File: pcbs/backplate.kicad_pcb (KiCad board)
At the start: 2 copper layers, 171.6 x 164.6 mm, 9 parts

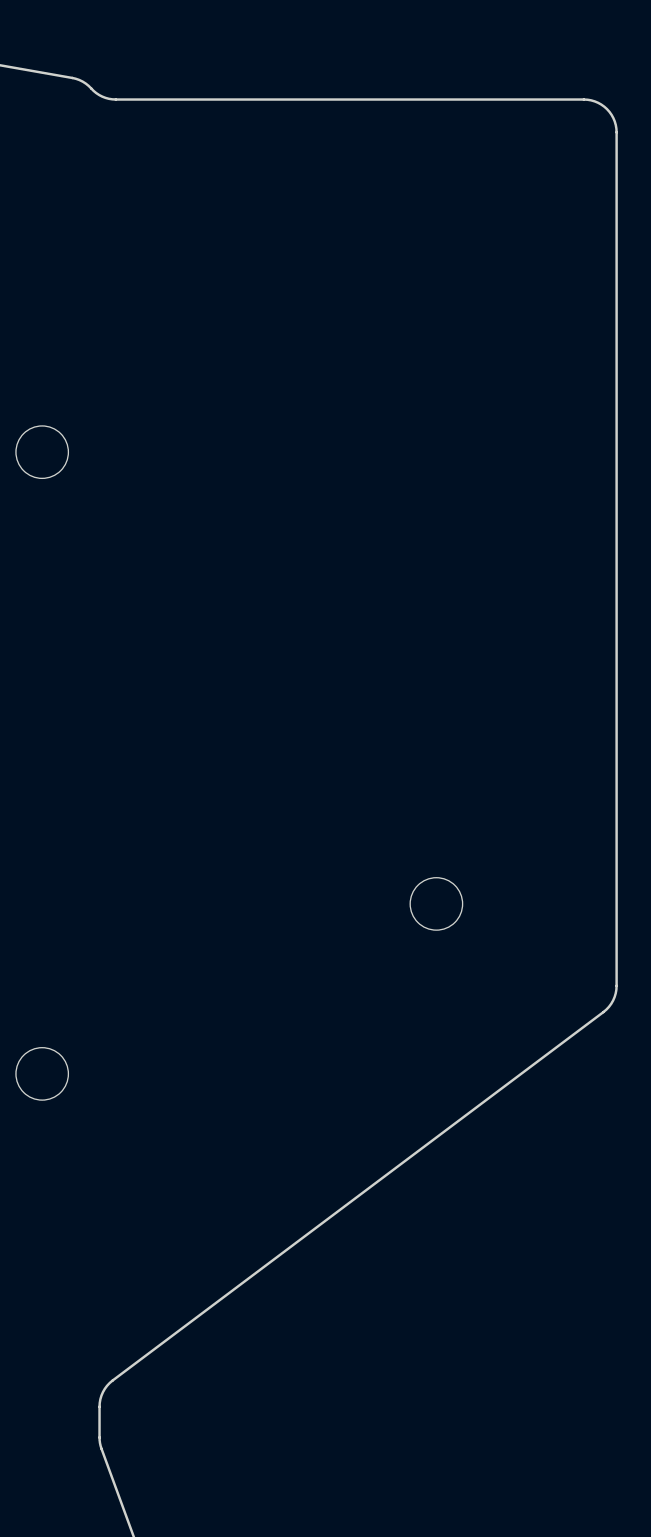
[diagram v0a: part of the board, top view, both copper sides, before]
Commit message: Tweaked layout, moved battery connector
shrinks the overall PCB by shrinking the mcu_padding
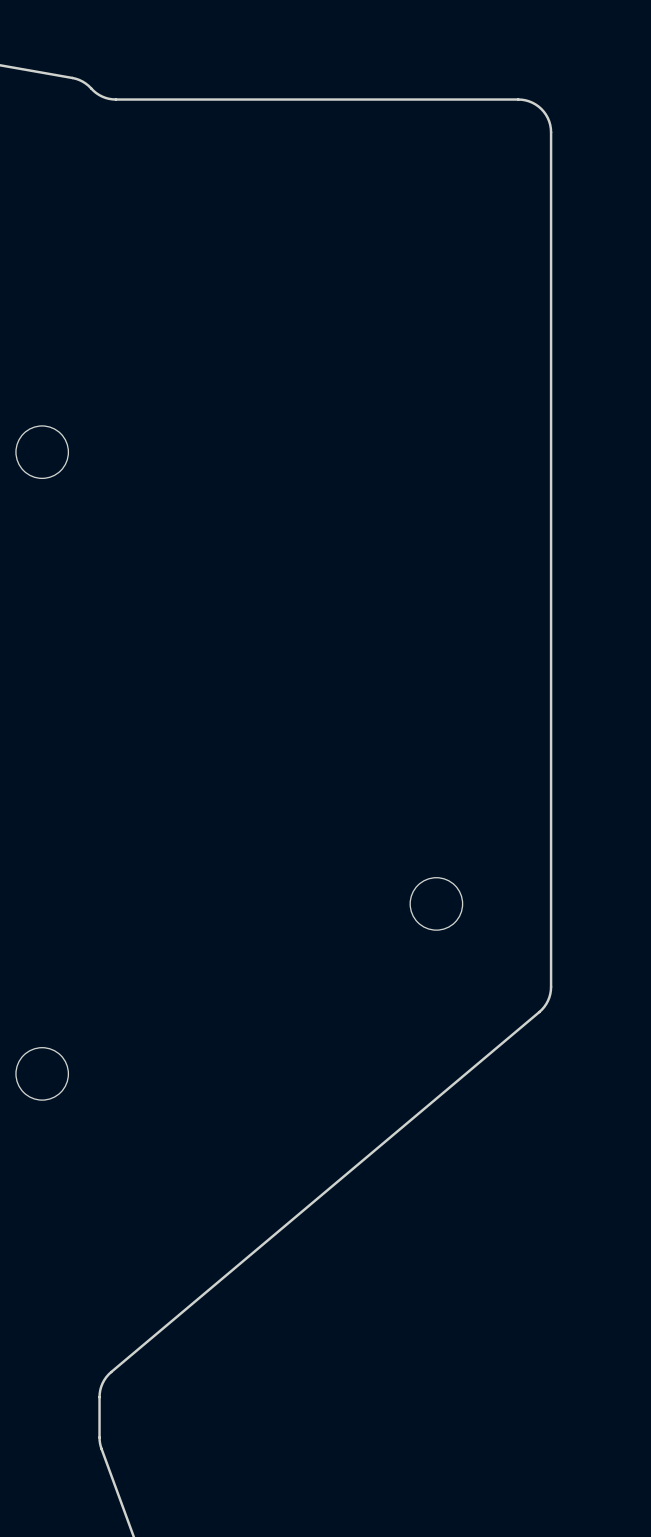
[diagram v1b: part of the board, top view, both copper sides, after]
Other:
- board size 171.6 x 164.6 mm -> 167.6 x 164.6 mm
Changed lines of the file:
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@@
     )
   )
-  (gr_line (start 178.0171124 37.000000010135274) (end 206.5875 37) (layer Edge.Cuts) (stroke (width 0.15) (type default)))
-(gr_line (start 208.5875 39) (end 208.5875 91.10053593324398) (layer Edge.Cuts) (stroke (width 0.15) (type default)))
-(gr_line (start 207.788186048012 92.7000211972028) (end 177.82431395198802 115.19300829341381) (layer Edge.Cuts) (stroke (width 0.15) (type default)))
-(gr_arc (start 208.5875 39) (mid 208.00171360000002 37.5857864) (end 206.5875 37) (layer Edge.Cuts) (stroke (width 0.15) (type default)))
-(gr_arc (start 207.788186 92.70002113324398) (mid 208.3765461 91.99457953324398) (end 208.5874999 91.10053593324398) (layer Edge.Cuts) (stroke (width 0.15) (type default)))
+  (gr_line (start 178.0171124 37.000000010074345) (end 202.5875 37) (layer Edge.Cuts) (stroke (width 0.15) (type default)))
+(gr_line (start 204.5875 39) (end 204.5875 91.16862729489486) (layer Edge.Cuts) (stroke (width 0.15) (type default)))
+(gr_line (start 203.87463864141816 92.6994029441529) (end 177.73786135858182 114.6762727315228) (layer Edge.Cuts) (stroke (width 0.15) (type default)))
+(gr_arc (start 204.5875 39) (mid 204.00171360000002 37.5857864) (end 202.5875 37) (layer Edge.Cuts) (stroke (width 0.15) (type default)))
+(gr_arc (start 203.8746386 92.69940299489487) (mid 204.4005468 92.01293849489487) (end 204.5875 91.16862739489486) (layer Edge.Cuts) (stroke (width 0.15) (type default)))
 (gr_line (start 36.975 136.025) (end 36.975 37.72908083684211) (layer Edge.Cuts) (stroke (width 0.15) (type default)))
 (gr_line (start 38.714091 35.746172236842106) (end 74.84941700000002 30.991524078947368) (layer Edge.Cuts) (stroke (width 0.15) (type default)))
@@
 (gr_line (start 94.23375318 25.975) (end 119.85089120000002 25.975) (layer Edge.Cuts) (stroke (width 0.15) (type default)))
 (gr_line (start 120.19649020000003 26.005086000000006) (end 175.370599 35.68475421052632) (layer Edge.Cuts) (stroke (width 0.15) (type default)))
-(gr_line (start 177.025 116.79249355737267) (end 177.025 118.67001579396174) (layer Edge.Cuts) (stroke (width 0.15) (type default)))
+(gr_line (start 177.025 116.20704838078086) (end 177.025 118.67001579396174) (layer Edge.Cuts) (stroke (width 0.15) (type default)))
 (gr_line (start 177.14716532046876 119.35830114980621) (end 192.4369873760196 161.0732105192838) (layer Edge.Cuts) (stroke (width 0.15) (type default)))
 (gr_line (start 191.84472794572866 163.2935847338106) (end 159.94187652195464 190.06325555278073) (layer Edge.Cuts) (stroke (width 0.15) (type default)))
@@
 (gr_arc (start 81.76624681999995 138.025) (mid 82.02286121999995 138.0084689) (end 82.27523341999995 137.95914910000002) (layer Edge.Cuts) (stroke (width 0.15) (type default)))
 (gr_arc (start 36.975 136.025) (mid 37.5607864 137.43921360000002) (end 38.975 138.025) (layer Edge.Cuts) (stroke (width 0.15) (type default)))
-(gr_arc (start 177.82431400000002 115.19300835737266) (mid 177.2359539 115.89844995737266) (end 177.0250001 116.79249355737267) (layer Edge.Cuts) (stroke (width 0.15) (type default)))
+(gr_arc (start 177.7378614 114.67627268078085) (mid 177.2119532 115.36273718078085) (end 177.025 116.20704828078087) (layer Edge.Cuts) (stroke (width 0.15) (type default)))
 (gr_arc (start 176.5210562 36.32733411052631) (mid 177.1969503 36.82409821052631) (end 178.0171124 37.00000001052631) (layer Edge.Cuts) (stroke (width 0.15) (type default)))
 )

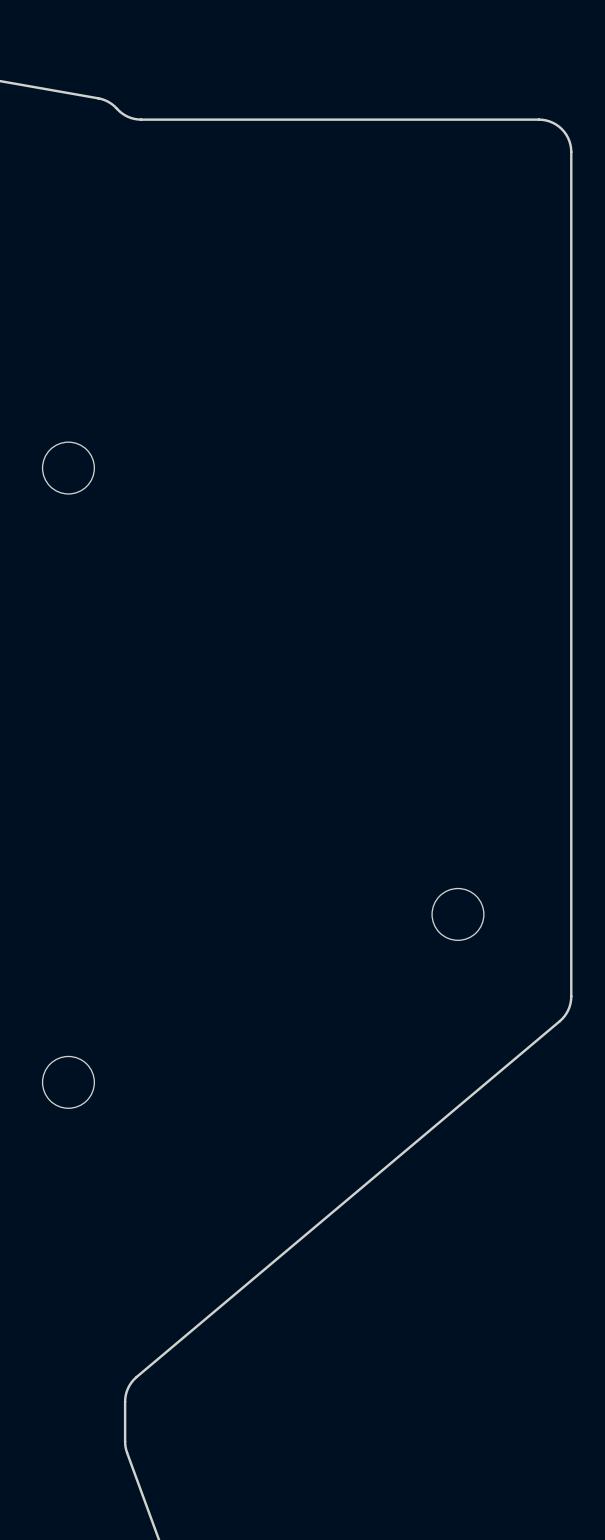
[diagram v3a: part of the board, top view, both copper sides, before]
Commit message: fully define display location with points and show on preview. Rotate encoder footprint
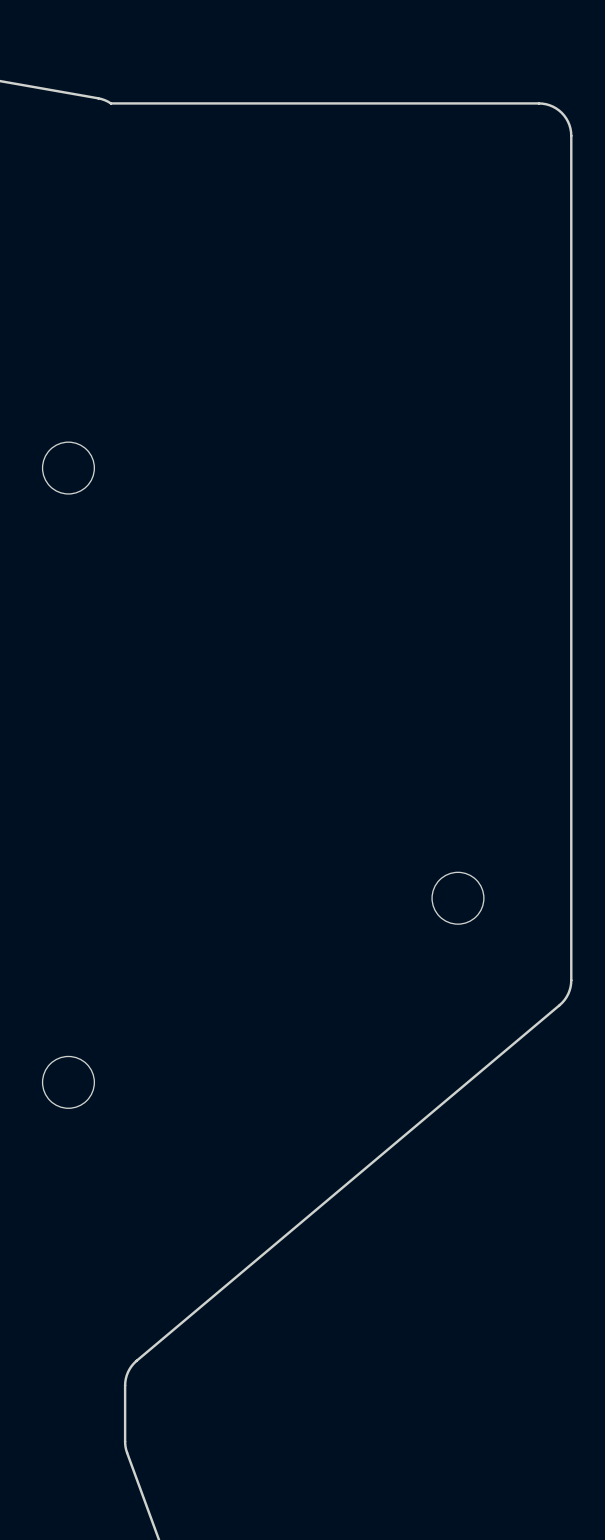
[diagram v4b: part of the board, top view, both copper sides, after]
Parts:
- moved MH9 1.00 mm to (197.6, 85.1)
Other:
- outline, holes or cut-outs redrawn
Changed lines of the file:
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@@
   (footprint "ceoloide:mounting_hole_npth"
     (layer "F.Cu")
-    (at 197.5875 86.1 0)
+    (at 197.5875 85.1 0)
     (property "Reference" "MH9"
       (at 0 2.55 0)
@@
     )
   )
-  (gr_line (start 178.0171124 37.000000010074345) (end 202.5875 37) (layer Edge.Cuts) (stroke (width 0.15) (type default)))
-(gr_line (start 204.5875 39) (end 204.5875 91.16862729489486) (layer Edge.Cuts) (stroke (width 0.15) (type default)))
-(gr_line (start 203.87463864141816 92.6994029441529) (end 177.73786135858182 114.6762727315228) (layer Edge.Cuts) (stroke (width 0.15) (type default)))
-(gr_arc (start 204.5875 39) (mid 204.00171360000002 37.5857864) (end 202.5875 37) (layer Edge.Cuts) (stroke (width 0.15) (type default)))
-(gr_arc (start 203.8746386 92.69940299489487) (mid 204.4005468 92.01293849489487) (end 204.5875 91.16862739489486) (layer Edge.Cuts) (stroke (width 0.15) (type default)))
+  (gr_line (start 176.1484203 36.00000001052631) (end 202.5875 36) (layer Edge.Cuts) (stroke (width 0.15) (type default)))
+(gr_line (start 204.5875 38) (end 204.5875 90.16862729489486) (layer Edge.Cuts) (stroke (width 0.15) (type default)))
+(gr_line (start 203.87463864141816 91.6994029441529) (end 177.73786135858182 113.6762727315228) (layer Edge.Cuts) (stroke (width 0.15) (type default)))
+(gr_arc (start 204.5875 38) (mid 204.00171360000002 36.5857864) (end 202.5875 36) (layer Edge.Cuts) (stroke (width 0.15) (type default)))
+(gr_arc (start 203.8746386 91.69940299489487) (mid 204.4005468 91.01293849489487) (end 204.5875 90.16862739489486) (layer Edge.Cuts) (stroke (width 0.15) (type default)))
 (gr_line (start 36.975 136.025) (end 36.975 37.72908083684211) (layer Edge.Cuts) (stroke (width 0.15) (type default)))
 (gr_line (start 38.714091 35.746172236842106) (end 74.84941700000002 30.991524078947368) (layer Edge.Cuts) (stroke (width 0.15) (type default)))
@@
 (gr_line (start 94.23375318 25.975) (end 119.85089120000002 25.975) (layer Edge.Cuts) (stroke (width 0.15) (type default)))
 (gr_line (start 120.19649020000003 26.005086000000006) (end 175.370599 35.68475421052632) (layer Edge.Cuts) (stroke (width 0.15) (type default)))
-(gr_line (start 177.025 116.20704838078086) (end 177.025 118.67001579396174) (layer Edge.Cuts) (stroke (width 0.15) (type default)))
+(gr_line (start 177.025 115.20704838078086) (end 177.025 118.67001579396174) (layer Edge.Cuts) (stroke (width 0.15) (type default)))
 (gr_line (start 177.14716532046876 119.35830114980621) (end 192.4369873760196 161.0732105192838) (layer Edge.Cuts) (stroke (width 0.15) (type default)))
 (gr_line (start 191.84472794572866 163.2935847338106) (end 159.94187652195464 190.06325555278073) (layer Edge.Cuts) (stroke (width 0.15) (type default)))
@@
 (gr_arc (start 94.23375318 25.975) (mid 93.97713877999999 25.991531100000003) (end 93.72476658 26.040850900000002) (layer Edge.Cuts) (stroke (width 0.15) (type default)))
 (gr_arc (start 120.19649020000003 26.005086000000002) (mid 120.02434420000002 25.9825357) (end 119.85089120000002 25.975) (layer Edge.Cuts) (stroke (width 0.15) (type default)))
-(gr_arc (start 176.5210562 36.32733411052631) (mid 176.0002696 35.90857281052631) (end 175.370599 35.68475421052631) (layer Edge.Cuts) (stroke (width 0.15) (type default)))
+(gr_arc (start 176.1484203 36.00000001052631) (mid 175.7762319 35.80111741052631) (end 175.370599 35.68475421052631) (layer Edge.Cuts) (stroke (width 0.15) (type default)))
 (gr_arc (start 177.025 118.67001579396174) (mid 177.0557781 119.01953729396173) (end 177.1471653 119.35830119396174) (layer Edge.Cuts) (stroke (width 0.15) (type default)))
 (gr_arc (start 191.84472799648833 163.2935847751282) (mid 192.49158799648833 162.27695087512822) (end 192.4369874964883 161.0732104751282) (layer Edge.Cuts) (stroke (width 0.15) (type default)))
@@
 (gr_arc (start 81.76624681999995 138.025) (mid 82.02286121999995 138.0084689) (end 82.27523341999995 137.95914910000002) (layer Edge.Cuts) (stroke (width 0.15) (type default)))
 (gr_arc (start 36.975 136.025) (mid 37.5607864 137.43921360000002) (end 38.975 138.025) (layer Edge.Cuts) (stroke (width 0.15) (type default)))
-(gr_arc (start 177.7378614 114.67627268078085) (mid 177.2119532 115.36273718078085) (end 177.025 116.20704828078087) (layer Edge.Cuts) (stroke (width 0.15) (type default)))
-(gr_arc (start 176.5210562 36.32733411052631) (mid 177.1969503 36.82409821052631) (end 178.0171124 37.00000001052631) (layer Edge.Cuts) (stroke (width 0.15) (type default)))
+(gr_arc (start 177.7378614 113.67627268078085) (mid 177.2119532 114.36273718078085) (end 177.025 115.20704828078087) (layer Edge.Cuts) (stroke (width 0.15) (type default)))
 )
